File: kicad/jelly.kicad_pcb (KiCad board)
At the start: 2 copper layers, 59.9 x 32.9 mm, 17 parts, among them M1 PAGER_MOTOR, M2 PAGER_MOTOR, P1 CONN_01X01, P2 CONN_01X01, P3 CONN_01X01, P4 CONN_01X01, P5 CONN_01X01, P6 CONN_01X01, P7 CONN_01X01, P8 CONN_01X01

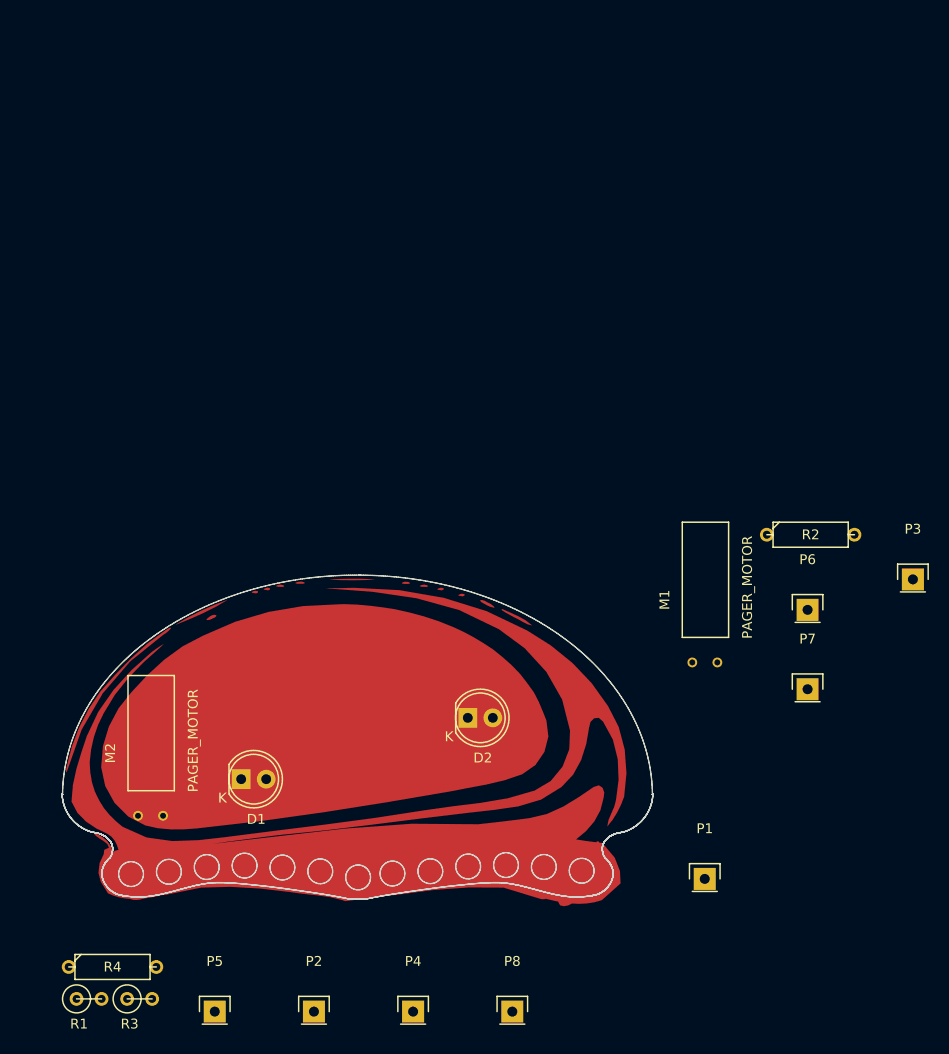
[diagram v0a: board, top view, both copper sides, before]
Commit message: Remove holes from jelly pads
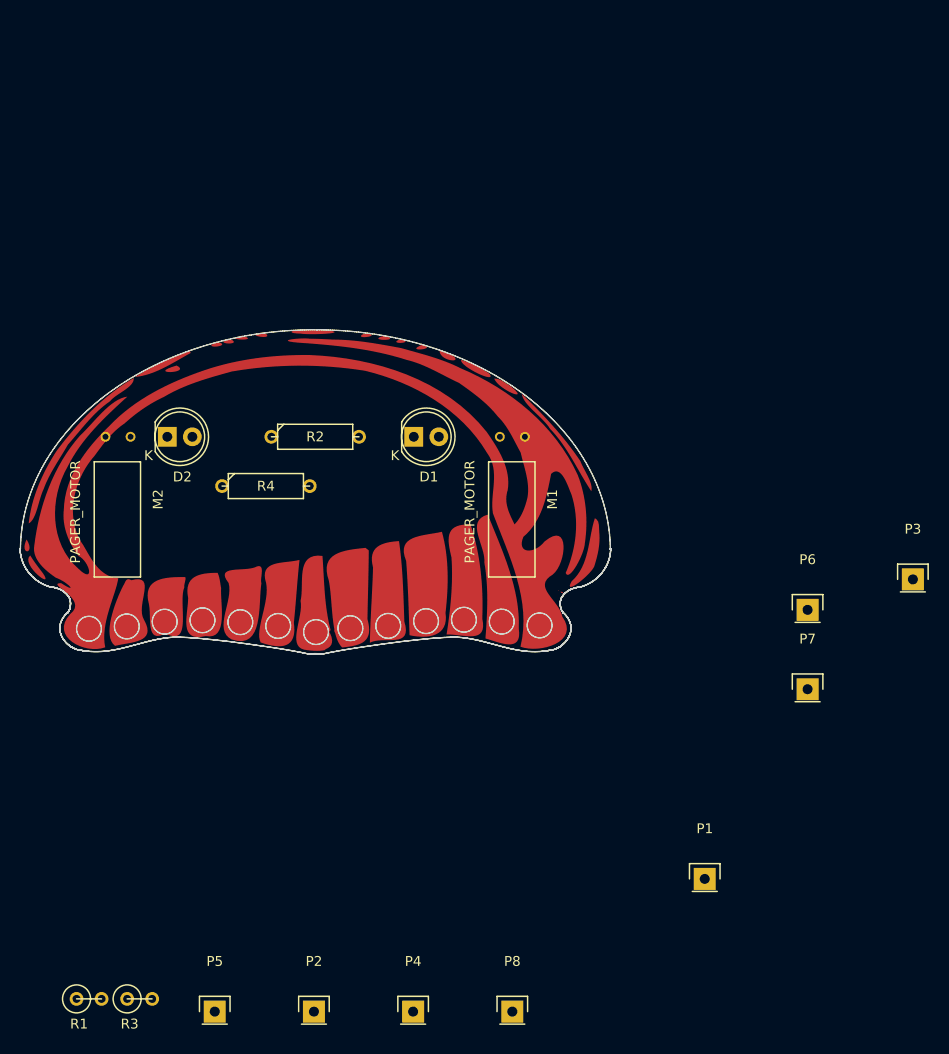
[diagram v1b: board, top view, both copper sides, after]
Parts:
- moved R2 51.2 mm to (150.0, 75.0)
- moved R4 51.2 mm to (145.0, 80.0)
- moved D2 41.7 mm to (135.0, 75.0)
- moved D1 38.9 mm to (160.0, 75.0)
- moved M2 38.6 mm to (130.0, 75.0), turned to 180 degrees
- moved M1 30.1 mm to (170.0, 75.0), turned to 180 degrees
- moved DNP1 25.6 mm to (150.0, 80.0)
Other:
- outline, holes or cut-outs redrawn

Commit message: Play with layout
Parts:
- moved R3 67.5 mm to (158.7, 70.0), turned to 180 degrees
- moved R1 63.1 mm to (138.8, 70.0)
- moved D2 12.1 mm to (134.7, 87.1)
- moved R4 8.79 mm to (137.8, 74.9)
- moved R2 7.86 mm to (157.9, 74.8)
- moved D1 7.78 mm to (161.3, 82.7), turned to 180 degrees
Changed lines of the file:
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@@
     (links 17)
     (no_connects 17)
-    (area 124.1 83.39 215.656667 135.629904)
+    (area 119.831056 58.505144 215.656667 135.629904)
     (thickness 1.6)
     (drawings 0)
@@
   )
   (module KiCad/LEDs.pretty:LED-5MM (layer F.Cu)
-    (at 160 75)
+    (at 161.29 82.677 180)
     (descr "LED 5mm round vertical")
     (tags "LED 5mm round vertical")
-    (fp_text reference D1 (at 1.524 4.064) (layer F.SilkS)
+    (fp_text reference D1 (at 1.524 4.064 180) (layer F.SilkS)
+      (effects (font (size 1 1) (thickness 0.15)))
+    )
+    (fp_text value LED (at 1.524 -3.937 180) (layer F.Fab)
+      (effects (font (size 1 1) (thickness 0.15)))
+    )
+    (fp_line (start -1.5 -1.55) (end -1.5 1.55) (layer F.CrtYd) (width 0.05))
+    (fp_arc (start 1.3 0) (end -1.5 1.55) (angle -302) (layer F.CrtYd) (width 0.05))
+    (fp_arc (start 1.27 0) (end -1.23 -1.5) (angle 297.5) (layer F.SilkS) (width 0.15))
+    (fp_line (start -1.23 1.5) (end -1.23 -1.5) (layer F.SilkS) (width 0.15))
+    (fp_circle (center 1.27 0) (end 0.97 -2.5) (layer F.SilkS) (width 0.15))
+    (fp_text user K (at -1.905 1.905 180) (layer F.SilkS)
+      (effects (font (size 1 1) (thickness 0.15)))
+    )
+    (pad 1 thru_hole rect (at 0 0 270) (size 2 1.9) (drill 1.00076) (layers *.Cu *.Mask F.SilkS)
+      (net 1 VCC))
+    (pad 2 thru_hole circle (at 2.54 0 180) (size 1.9 1.9) (drill 1.00076) (layers *.Cu *.Mask F.SilkS)
+      (net 2 "Net-(D1-Pad2)"))
+    (model LEDs.3dshapes/LED-5MM.wrl
+      (at (xyz 0.05 0 0))
+      (scale (xyz 1 1 1))
+      (rotate (xyz 0 0 90))
+    )
+  )
+  (module KiCad/LEDs.pretty:LED-5MM (layer F.Cu)
+    (at 134.6708 87.122)
+    (descr "LED 5mm round vertical")
+    (tags "LED 5mm round vertical")
+    (fp_text reference D2 (at 1.524 4.064) (layer F.SilkS)
       (effects (font (size 1 1) (thickness 0.15)))
     )
@@
       (net 1 VCC))
     (pad 2 thru_hole circle (at 2.54 0) (size 1.9 1.9) (drill 1.00076) (layers *.Cu *.Mask F.SilkS)
-      (net 2 "Net-(D1-Pad2)"))
-    (model LEDs.3dshapes/LED-5MM.wrl
-      (at (xyz 0.05 0 0))
-      (scale (xyz 1 1 1))
-      (rotate (xyz 0 0 90))
-    )
-  )
-  (module KiCad/LEDs.pretty:LED-5MM (layer F.Cu)
-    (at 135 75)
-    (descr "LED 5mm round vertical")
-    (tags "LED 5mm round vertical")
-    (fp_text reference D2 (at 1.524 4.064) (layer F.SilkS)
-      (effects (font (size 1 1) (thickness 0.15)))
-    )
-    (fp_text value LED (at 1.524 -3.937) (layer F.Fab)
-      (effects (font (size 1 1) (thickness 0.15)))
-    )
-    (fp_line (start -1.5 -1.55) (end -1.5 1.55) (layer F.CrtYd) (width 0.05))
-    (fp_arc (start 1.3 0) (end -1.5 1.55) (angle -302) (layer F.CrtYd) (width 0.05))
-    (fp_arc (start 1.27 0) (end -1.23 -1.5) (angle 297.5) (layer F.SilkS) (width 0.15))
-    (fp_line (start -1.23 1.5) (end -1.23 -1.5) (layer F.SilkS) (width 0.15))
-    (fp_circle (center 1.27 0) (end 0.97 -2.5) (layer F.SilkS) (width 0.15))
-    (fp_text user K (at -1.905 1.905) (layer F.SilkS)
-      (effects (font (size 1 1) (thickness 0.15)))
-    )
-    (pad 1 thru_hole rect (at 0 0 90) (size 2 1.9) (drill 1.00076) (layers *.Cu *.Mask F.SilkS)
-      (net 1 VCC))
-    (pad 2 thru_hole circle (at 2.54 0) (size 1.9 1.9) (drill 1.00076) (layers *.Cu *.Mask F.SilkS)
       (net 3 "Net-(D2-Pad2)"))
     (model LEDs.3dshapes/LED-5MM.wrl
@@
   )
   (module KiCad/Discret.pretty:R1 (layer F.Cu)
-    (at 127.064904 132.014904)
+    (at 138.81 70)
     (descr "Resistance verticale")
     (tags R)
@@
   )
   (module KiCad/Discret.pretty:R3-5 (layer F.Cu)
-    (at 150 75)
+    (at 157.861 74.7776)
     (fp_text reference R2 (at 0 0) (layer F.SilkS)
       (effects (font (size 1 1) (thickness 0.15)))
@@
   )
   (module KiCad/Discret.pretty:R1 (layer F.Cu)
-    (at 132.194904 132.014904)
+    (at 158.73 70 180)
     (descr "Resistance verticale")
     (tags R)
-    (fp_text reference R3 (at -1.016 2.54) (layer F.SilkS)
-      (effects (font (size 1 1) (thickness 0.15)))
-    )
-    (fp_text value 220 (at -1.143 2.54) (layer F.Fab)
+    (fp_text reference R3 (at -1.016 2.54 180) (layer F.SilkS)
+      (effects (font (size 1 1) (thickness 0.15)))
+    )
+    (fp_text value 220 (at -1.143 2.54 180) (layer F.Fab)
       (effects (font (size 1 1) (thickness 0.15)))
     )
     (fp_line (start -1.27 0) (end 1.27 0) (layer F.SilkS) (width 0.15))
     (fp_circle (center -1.27 0) (end -0.635 1.27) (layer F.SilkS) (width 0.15))
-    (pad 1 thru_hole circle (at -1.27 0) (size 1.397 1.397) (drill 0.8128) (layers *.Cu *.Mask F.SilkS)
-      (net 1 VCC))
-    (pad 2 thru_hole circle (at 1.27 0) (size 1.397 1.397) (drill 0.8128) (layers *.Cu *.Mask F.SilkS)
+    (pad 1 thru_hole circle (at -1.27 0 180) (size 1.397 1.397) (drill 0.8128) (layers *.Cu *.Mask F.SilkS)
+      (net 1 VCC))
+    (pad 2 thru_hole circle (at 1.27 0 180) (size 1.397 1.397) (drill 0.8128) (layers *.Cu *.Mask F.SilkS)
       (net 7 "Net-(Q2-Pad2)"))
     (model Discret.3dshapes/R1.wrl
@@
   )
   (module KiCad/Discret.pretty:R3-5 (layer F.Cu)
-    (at 145 80)
+    (at 137.8204 74.93)
     (fp_text reference R4 (at 0 0) (layer F.SilkS)
       (effects (font (size 1 1) (thickness 0.15)))

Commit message: Layout some components
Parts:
- added P10: CONN_01X01, footprints:hole, F.Cu at (165.0, 82.5)
- added P9: CONN_01X01, footprints:hole, F.Cu at (135.0, 82.5)
- added Q1: 2N7000, KiCad/TO_SOT_Packages_THT.pretty:TO-92_Rugged, F.Cu at (150.0, 82.5)
- added Q2: 2N7000, KiCad/TO_SOT_Packages_THT.pretty:TO-92_Rugged, F.Cu at (145.0, 80.0)
- moved D2 4.17 mm to (138.8, 87.1), turned to 270 degrees
- moved D1 1.15 mm to (160.5, 83.5), turned to 270 degrees
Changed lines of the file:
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@@
 (kicad_pcb (version 4) (host pcbnew 4.0.3+e1-6302~38~ubuntu14.04.1-stable)
   (general
-    (links 17)
-    (no_connects 17)
-    (area 119.831056 58.505144 215.656667 135.629904)
+    (links 22)
+    (no_connects 22)
+    (area 119.831056 58.505144 215.656667 135.280001)
     (thickness 1.6)
     (drawings 0)
     (tracks 0)
     (zones 0)
-    (modules 17)
-    (nets 8)
+    (modules 21)
+    (nets 11)
   )
   (page A4)
@@
   (net 6 "Net-(Q1-Pad2)")
   (net 7 "Net-(Q2-Pad2)")
+  (net 8 "Net-(P9-Pad1)")
+  (net 9 "Net-(P10-Pad1)")
+  (net 10 GND)
   (net_class Default "This is the default net class."
     (clearance 0.2)
@@
     (uvia_dia 0.3)
     (uvia_drill 0.1)
+    (add_net GND)
     (add_net "Net-(D1-Pad2)")
     (add_net "Net-(D2-Pad2)")
+    (add_net "Net-(P10-Pad1)")
+    (add_net "Net-(P9-Pad1)")
     (add_net "Net-(Q1-Pad2)")
     (add_net "Net-(Q2-Pad2)")
@@
   )
   (module KiCad/LEDs.pretty:LED-5MM (layer F.Cu)
-    (at 161.29 82.677 180)
+    (at 160.4518 83.4644 270)
     (descr "LED 5mm round vertical")
     (tags "LED 5mm round vertical")
-    (fp_text reference D1 (at 1.524 4.064 180) (layer F.SilkS)
+    (fp_text reference D1 (at 1.524 4.064 270) (layer F.SilkS)
       (effects (font (size 1 1) (thickness 0.15)))
     )
-    (fp_text value LED (at 1.524 -3.937 180) (layer F.Fab)
+    (fp_text value LED (at 1.524 -3.937 270) (layer F.Fab)
       (effects (font (size 1 1) (thickness 0.15)))
     )
@@
     (fp_line (start -1.23 1.5) (end -1.23 -1.5) (layer F.SilkS) (width 0.15))
     (fp_circle (center 1.27 0) (end 0.97 -2.5) (layer F.SilkS) (width 0.15))
-    (fp_text user K (at -1.905 1.905 180) (layer F.SilkS)
+    (fp_text user K (at -1.905 1.905 270) (layer F.SilkS)
       (effects (font (size 1 1) (thickness 0.15)))
     )
-    (pad 1 thru_hole rect (at 0 0 270) (size 2 1.9) (drill 1.00076) (layers *.Cu *.Mask F.SilkS)
+    (pad 1 thru_hole rect (at 0 0) (size 2 1.9) (drill 1.00076) (layers *.Cu *.Mask F.SilkS)
       (net 1 VCC))
-    (pad 2 thru_hole circle (at 2.54 0 180) (size 1.9 1.9) (drill 1.00076) (layers *.Cu *.Mask F.SilkS)
+    (pad 2 thru_hole circle (at 2.54 0 270) (size 1.9 1.9) (drill 1.00076) (layers *.Cu *.Mask F.SilkS)
       (net 2 "Net-(D1-Pad2)"))
     (model LEDs.3dshapes/LED-5MM.wrl
@@
   )
   (module KiCad/LEDs.pretty:LED-5MM (layer F.Cu)
-    (at 134.6708 87.122)
+    (at 138.8364 87.1474 270)
     (descr "LED 5mm round vertical")
     (tags "LED 5mm round vertical")
-    (fp_text reference D2 (at 1.524 4.064) (layer F.SilkS)
+    (fp_text reference D2 (at 1.524 4.064 270) (layer F.SilkS)
       (effects (font (size 1 1) (thickness 0.15)))
     )
-    (fp_text value LED (at 1.524 -3.937) (layer F.Fab)
+    (fp_text value LED (at 1.524 -3.937 270) (layer F.Fab)
       (effects (font (size 1 1) (thickness 0.15)))
     )
@@
     (fp_line (start -1.23 1.5) (end -1.23 -1.5) (layer F.SilkS) (width 0.15))
     (fp_circle (center 1.27 0) (end 0.97 -2.5) (layer F.SilkS) (width 0.15))
-    (fp_text user K (at -1.905 1.905) (layer F.SilkS)
+    (fp_text user K (at -1.905 1.905 270) (layer F.SilkS)
       (effects (font (size 1 1) (thickness 0.15)))
     )
-    (pad 1 thru_hole rect (at 0 0 90) (size 2 1.9) (drill 1.00076) (layers *.Cu *.Mask F.SilkS)
+    (pad 1 thru_hole rect (at 0 0) (size 2 1.9) (drill 1.00076) (layers *.Cu *.Mask F.SilkS)
       (net 1 VCC))
-    (pad 2 thru_hole circle (at 2.54 0) (size 1.9 1.9) (drill 1.00076) (layers *.Cu *.Mask F.SilkS)
+    (pad 2 thru_hole circle (at 2.54 0 270) (size 1.9 1.9) (drill 1.00076) (layers *.Cu *.Mask F.SilkS)
       (net 3 "Net-(D2-Pad2)"))
     (model LEDs.3dshapes/LED-5MM.wrl
@@
       (xy 24.884967 10.694322)) (layer F.Cu) (width 0))
   )
+  (module footprints:hole (layer F.Cu)
+    (at 135 82.5)
+    (fp_text reference P9 (at 0 0.5) (layer F.SilkS)
+      (effects (font (size 1 1) (thickness 0.15)))
+    )
+    (fp_text value CONN_01X01 (at 0 -0.5) (layer F.Fab)
+      (effects (font (size 1 1) (thickness 0.15)))
+    )
+    (pad 1 thru_hole circle (at 0 0) (size 4 4) (drill 3) (layers *.Cu *.Mask)
+      (net 8 "Net-(P9-Pad1)"))
+  )
+  (module footprints:hole (layer F.Cu)
+    (at 165 82.5)
+    (fp_text reference P10 (at 0 0.5) (layer F.SilkS)
+      (effects (font (size 1 1) (thickness 0.15)))
+    )
+    (fp_text value CONN_01X01 (at 0 -0.5) (layer F.Fab)
+      (effects (font (size 1 1) (thickness 0.15)))
+    )
+    (pad 1 thru_hole circle (at 0 0) (size 4 4) (drill 3) (layers *.Cu *.Mask)
+      (net 9 "Net-(P10-Pad1)"))
+  )
+  (module KiCad/TO_SOT_Packages_THT.pretty:TO-92_Rugged (layer F.Cu)
+    (at 150 82.5)
+    (descr "TO-92 rugged, leads molded, wide, drill 1mm (see NXP sot054_po.pdf)")
+    (tags "to-92 sc-43 sc-43a sot54 PA33 transistor")
+    (fp_text reference Q1 (at 0 -6) (layer F.SilkS)
+      (effects (font (size 1 1) (thickness 0.15)))
+    )
+    (fp_text value 2N7000 (at 0 3) (layer F.Fab)
+      (effects (font (size 1 1) (thickness 0.15)))
+    )
+    (fp_arc (start 2.54 0) (end 0.49 -1.25) (angle 27.25399767) (layer F.SilkS) (width 0.15))
+    (fp_arc (start 2.54 0) (end 4.59 -1.25) (angle -27.25399767) (layer F.SilkS) (width 0.15))
+    (fp_arc (start 2.54 0) (end 0.84 1.7) (angle 12.99463195) (layer F.SilkS) (width 0.15))
+    (fp_arc (start 2.54 0) (end 4.24 1.7) (angle -12.99463195) (layer F.SilkS) (width 0.15))
+    (fp_line (start -1.75 1.95) (end -1.75 -4.3) (layer F.CrtYd) (width 0.05))
+    (fp_line (start -1.75 1.95) (end 6.85 1.95) (layer F.CrtYd) (width 0.05))
+    (fp_line (start 0.84 1.7) (end 4.24 1.7) (layer F.SilkS) (width 0.15))
+    (fp_line (start -1.75 -4.3) (end 6.85 -4.3) (layer F.CrtYd) (width 0.05))
+    (fp_line (start 6.85 1.95) (end 6.85 -4.3) (layer F.CrtYd) (width 0.05))
+    (pad 2 thru_hole oval (at 2.54 -2.54 90) (size 2.99974 1.99898) (drill 1) (layers *.Cu *.Mask F.SilkS)
+      (net 6 "Net-(Q1-Pad2)"))
+    (pad 1 thru_hole oval (at 0 0 90) (size 1.99898 2.99974) (drill 1) (layers *.Cu *.Mask F.SilkS)
+      (net 10 GND))
+    (pad 3 thru_hole oval (at 5.08 0 90) (size 1.99898 2.99974) (drill 1) (layers *.Cu *.Mask F.SilkS)
+      (net 4 Vout1))
+    (model TO_SOT_Packages_THT.3dshapes/TO-92_Rugged.wrl
+      (at (xyz 0.1 0 0))
+      (scale (xyz 1 1 1))
+      (rotate (xyz 0 0 -90))
+    )
+  )
+  (module KiCad/TO_SOT_Packages_THT.pretty:TO-92_Rugged (layer F.Cu)
+    (at 145 80 180)
+    (descr "TO-92 rugged, leads molded, wide, drill 1mm (see NXP sot054_po.pdf)")
+    (tags "to-92 sc-43 sc-43a sot54 PA33 transistor")
+    (fp_text reference Q2 (at 0 -6 180) (layer F.SilkS)
+      (effects (font (size 1 1) (thickness 0.15)))
+    )
+    (fp_text value 2N7000 (at 0 3 180) (layer F.Fab)
+      (effects (font (size 1 1) (thickness 0.15)))
+    )
+    (fp_arc (start 2.54 0) (end 0.49 -1.25) (angle 27.25399767) (layer F.SilkS) (width 0.15))
+    (fp_arc (start 2.54 0) (end 4.59 -1.25) (angle -27.25399767) (layer F.SilkS) (width 0.15))
+    (fp_arc (start 2.54 0) (end 0.84 1.7) (angle 12.99463195) (layer F.SilkS) (width 0.15))
+    (fp_arc (start 2.54 0) (end 4.24 1.7) (angle -12.99463195) (layer F.SilkS) (width 0.15))
+    (fp_line (start -1.75 1.95) (end -1.75 -4.3) (layer F.CrtYd) (width 0.05))
+    (fp_line (start -1.75 1.95) (end 6.85 1.95) (layer F.CrtYd) (width 0.05))
+    (fp_line (start 0.84 1.7) (end 4.24 1.7) (layer F.SilkS) (width 0.15))
+    (fp_line (start -1.75 -4.3) (end 6.85 -4.3) (layer F.CrtYd) (width 0.05))
+    (fp_line (start 6.85 1.95) (end 6.85 -4.3) (layer F.CrtYd) (width 0.05))
+    (pad 2 thru_hole oval (at 2.54 -2.54 270) (size 2.99974 1.99898) (drill 1) (layers *.Cu *.Mask F.SilkS)
+      (net 7 "Net-(Q2-Pad2)"))
+    (pad 1 thru_hole oval (at 0 0 270) (size 1.99898 2.99974) (drill 1) (layers *.Cu *.Mask F.SilkS)
+      (net 10 GND))
+    (pad 3 thru_hole oval (at 5.08 0 270) (size 1.99898 2.99974) (drill 1) (layers *.Cu *.Mask F.SilkS)
+      (net 5 Vout2))
+    (model TO_SOT_Packages_THT.3dshapes/TO-92_Rugged.wrl
+      (at (xyz 0.1 0 0))
+      (scale (xyz 1 1 1))
+      (rotate (xyz 0 0 -90))
+    )
+  )
 )

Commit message: Move things about
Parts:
- added BT1: BATTERY, KiCad/Connectors_JST.pretty:JST_PH_S2B-PH-K_02x2.00mm_Angled, F.Cu at (149.4, 75.6)
- added RV1: DUAL_POT, pelrun/libKiCad/footprint/w_pth_resistors.pretty:trimmer_alps_rk12l12c0-f20-c0, F.Cu at (146.5, 42.1)
- M1, M2: footprint pager_motor_custom -> footprints:pager_motor_custom
